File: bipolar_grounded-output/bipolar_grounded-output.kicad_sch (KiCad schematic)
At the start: 42 parts, among them J1 Conn_01x10_Pin, J10 Output, J11 Conn_Coaxial, J12 Conn_01x04_Pin, J2 Conn_01x10_Pin, J3 Conn_01x04_Pin, J4 Conn_01x05, J5 Conn_01x03, J6 Setpoint, J7 Monitor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

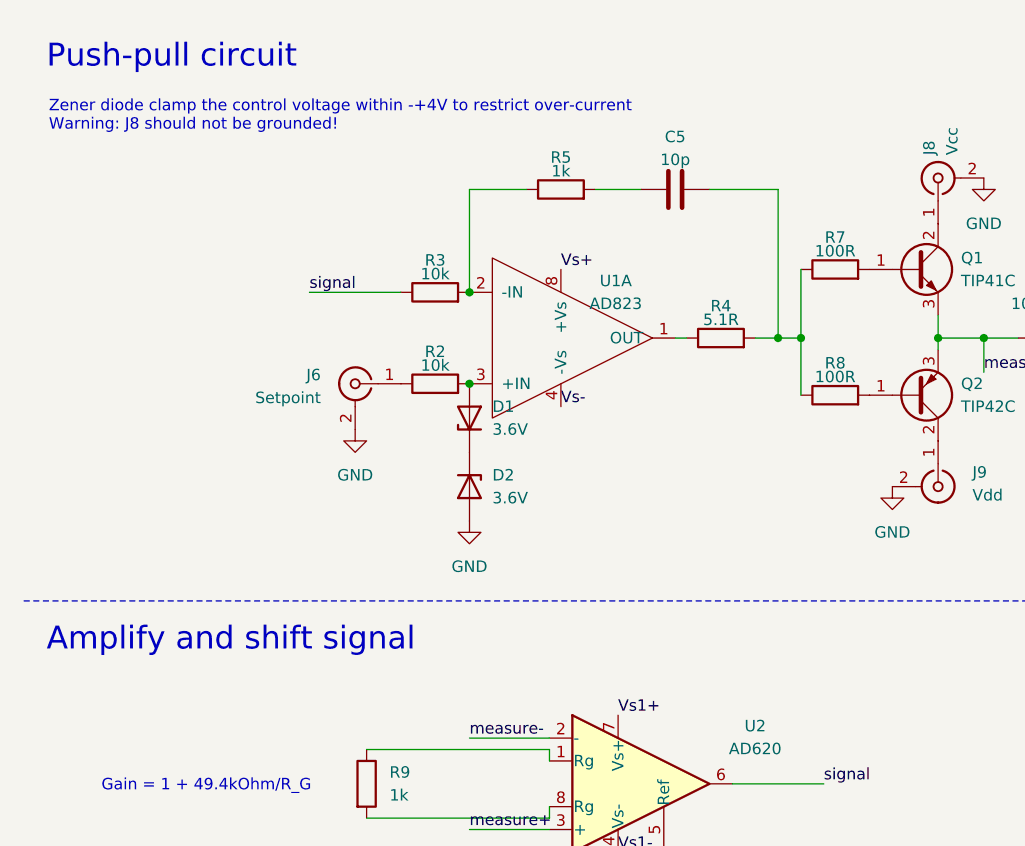
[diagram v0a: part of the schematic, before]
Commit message: add a grounded-output for bipolar current source
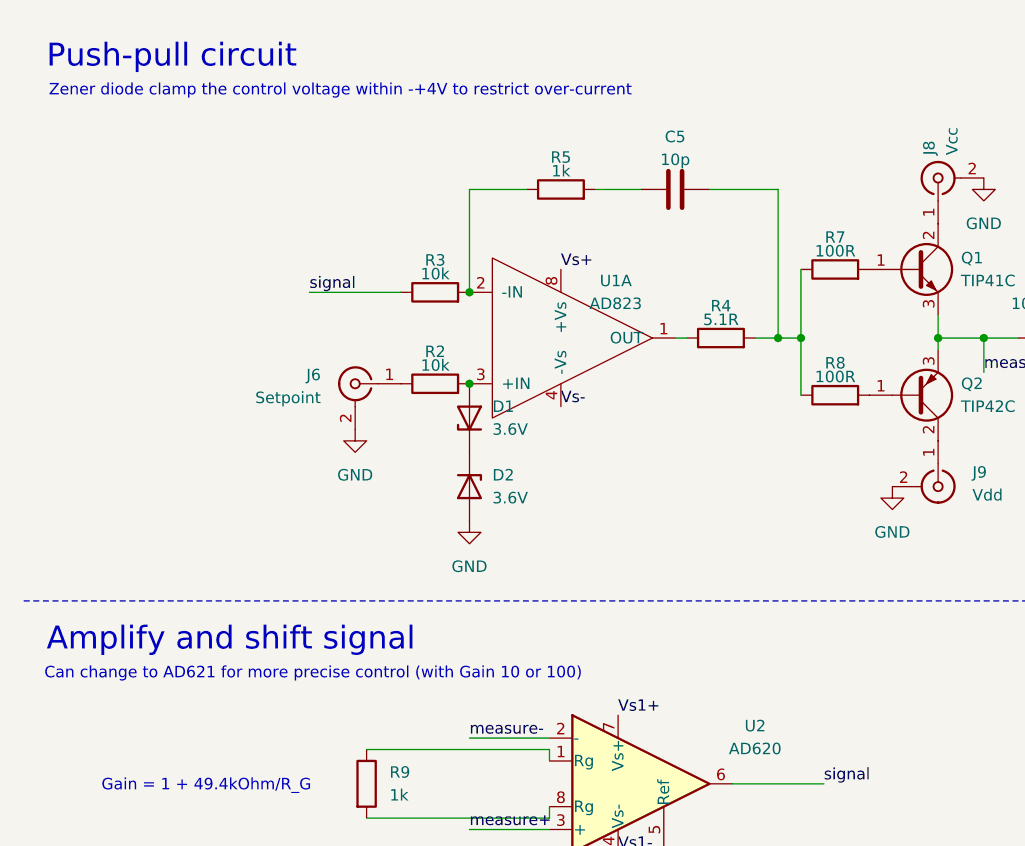
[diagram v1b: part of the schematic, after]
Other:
- note added: "Can change to AD621 for more precise control (with Gain 10 or 100)"
- note added: "Zener diode clamp the control voltage within -+4V to restrict over-current"
- note removed: "Zener diode clamp the control voltage within -+4V to restrict over-current Warning: J8 should not be grounded!"
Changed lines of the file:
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@@
 		)
 	)
-	(text "Zener diode clamp the control voltage within -+4V to restrict over-current\nWarning: J8 should not be grounded!"
+	(text "Zener diode clamp the control voltage within -+4V to restrict over-current"
 		(exclude_from_sim no)
-		(at 15.494 25.4 0)
+		(at 15.494 21.59 0)
 		(effects
 			(font
@@
 		(effects
 			(font
+				(size 1.27 1.27)
+			)
+			(justify left bottom)
+		)
+	)
+	(text "Can change to AD621 for more precise control (with Gain 10 or 100)"
+		(exclude_from_sim no)
+		(at 14.986 86.36 0)
+		(effects
+			(font

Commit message: layout PCB for grounded bipolar
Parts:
- removed J12, J3: Conn_01x04_Pin, Connector_JST:JST_PH_S4B-PH-K_1x04_P2.00mm_Horizontal, symbol Connector:Conn_01x04_Pin
- removed J5: Conn_01x03, Connector_Wire:SolderWire-0.75sqmm_1x03_P4.8mm_D1.25mm_OD2.3mm, symbol Connector_Generic:Conn_01x03
- added C10: 1n, Capacitor_THT:C_Disc_D5.0mm_W2.5mm_P5.00mm, symbol Device:C
- added J3: AD621 Gain or AD620 select Pin, Connector_PinHeader_2.54mm:PinHeader_1x03_P2.54mm_Vertical, symbol Connector:Conn_01x03_Pin
- added R10: 1k, Resistor_THT:R_Axial_DIN0207_L6.3mm_D2.5mm_P10.16mm_Horizontal, symbol Device:R
- D1, D2: value 3.6V -> 10V
- R1: footprint (none) -> Resistor_SMD:R_2512_6332Metric; LCSC (none) -> C500724
- R2: value 10k -> 1k; LCSC C57204 -> C57435
- R9: value 1k -> 510R; footprint (none) -> Resistor_THT:R_Axial_DIN0207_L6.3mm_D2.5mm_P10.16mm_Horizontal
- U2: footprint (none) -> Package_DIP:DIP-8_W7.62mm_Socket_LongPads
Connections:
- net GND: now also C10.1, R10.1
- net at R9.1: now also J3.1 (Pin_1); no longer U2.1 (Rg)
- net at R9.2, U2.8 (Rg): now also J3.3 (Pin_3)
- net at D1.2 (A), R2.2, U1.3 (+IN): now also C10.2
- net at J6.1 (In), R2.1: now also R10.2
- new net: J3.2 (Pin_2), U2.1 (Rg)
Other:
- note added: "AD620 Gain = 1 + 49.4kOhm/R_G, select 12 (for 510Ohm, Gain is around 100 -- 10V setpoint -> 1A current, can increase the resistor for larger current range); AD621 Gain = 10, do not connect; AD621 Gain = 100, select 23."
- note added: "Can change to AD621 for more precise control (with Gain 10 or 100). For AD621, use +-15V power supply instead of +-12V."
- note added: "Zener diode to clamp voltage can be choose based on needs. R2 and C10 forms a low pass filter around 100kHz"
- note removed: "Can change to AD621 for more precise control (with Gain 10 or 100)"
- note removed: "Gain = 1 + 49.4kOhm/R_G"
- note removed: "STEMMA QT I^{2}C connector"
- note removed: "Zener diode clamp the control voltage within -+4V to restrict over-current"
- moved on the sheet: C5, D1, D2, J10, J6, J8, J9, Q1, Q2, R1, R2, R3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

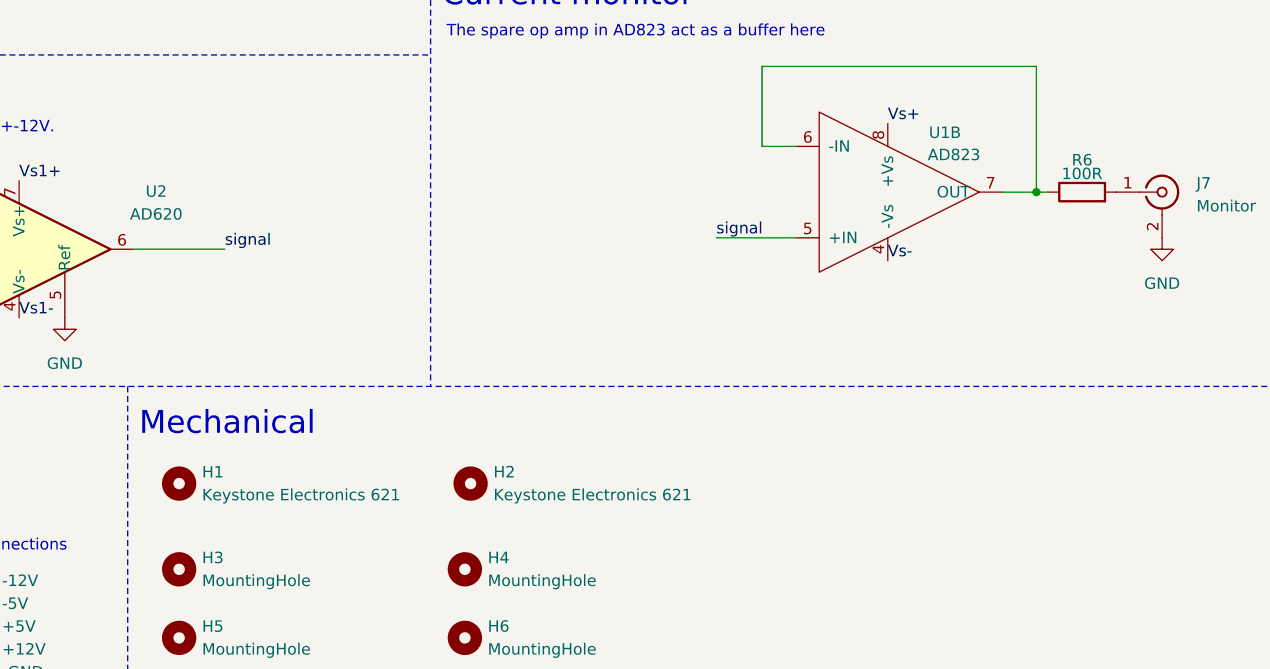
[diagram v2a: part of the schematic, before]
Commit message: update circuit with op amp power selection
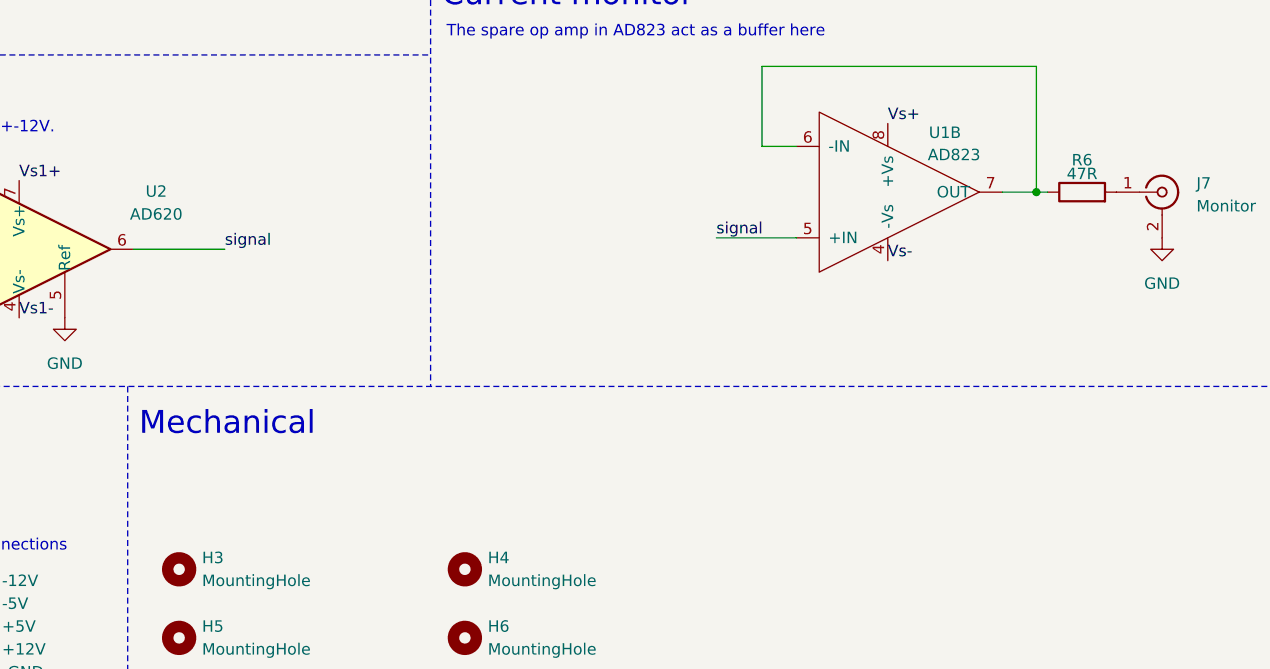
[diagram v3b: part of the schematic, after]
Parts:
- removed H1, H2: Keystone Electronics 621, matterwaves:Keystone 621, symbol Mechanical:MountingHole
- R6: value 100R -> 47R; LCSC C57438 -> C119296
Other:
- company: (none) -> Mueller Group, UC Berkeley
- title: ??? -> Bipolar current control (grounded output)
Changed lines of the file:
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@@
 	(paper "A4")
 	(title_block
-		(title "???")
-		(comment 1 "Designed by Jack Roth")
+		(title "Bipolar current control (grounded output)")
+		(company "Mueller Group, UC Berkeley")
 		(comment 2 "Compatible with Hammond Manufacturing series 1457")
 	)
@@
 	)
 	(symbol
-		(lib_id "Mechanical:MountingHole")
-		(at 169.545 125.095 0)
-		(unit 1)
-		(exclude_from_sim no)
-		(in_bom yes)
-		(on_board yes)
-		(dnp no)
-		(fields_autoplaced yes)
-		(property "Reference" "H2"
-			(at 172.085 123.825 0)
-			(effects
-				(font
-					(size 1.27 1.27)
-				)
-				(justify left)
-			)
-		)
-		(property "Value" "Keystone Electronics 621"
-			(at 172.085 126.365 0)
-			(effects
-				(font
-					(size 1.27 1.27)
-				)
-				(justify left)
-			)
-		)
-		(property "Footprint" "matterwaves:Keystone 621"
-			(at 169.545 125.095 0)
-			(effects
-				(font
-					(size 1.27 1.27)
-				)
-				(hide yes)
-			)
-		)
-		(property "Datasheet" "~"
-			(at 169.545 125.095 0)
-			(effects
-				(font
-					(size 1.27 1.27)
-				)
-				(hide yes)
-			)
-		)
-		(property "Description" "Mounting Hole without connection"
-			(at 169.545 125.095 0)
-			(effects
-				(font
-					(size 1.27 1.27)
-				)
-				(hide yes)
-			)
-		)
-		(property "Digikey PN" "36-621-ND"
-			(at 169.545 125.095 0)
-			(effects
-				(font
-					(size 1.27 1.27)
-				)
-				(hide yes)
-			)
-		)
-		(instances
-			(project "Hammond_1457_with_picoblade"
-				(path "/9c6abd11-1aac-4f08-8b79-cac116854bcb"
-					(reference "H2")
-					(unit 1)
-				)
-			)
-		)
-	)
-	(symbol
 		(lib_id "power:GND")
 		(at 62.23 60.96 0)
@@
 	)
 	(symbol
-		(lib_id "Mechanical:MountingHole")
-		(at 137.16 125.095 0)
-		(unit 1)
-		(exclude_from_sim no)
-		(in_bom yes)
-		(on_board yes)
-		(dnp no)
-		(fields_autoplaced yes)
-		(property "Reference" "H1"
-			(at 139.7 123.825 0)
-			(effects
-				(font
-					(size 1.27 1.27)
-				)
-				(justify left)
-			)
-		)
-		(property "Value" "Keystone Electronics 621"
-			(at 139.7 126.365 0)
-			(effects
-				(font
-					(size 1.27 1.27)
-				)
-				(justify left)
-			)
-		)
-		(property "Footprint" "matterwaves:Keystone 621"
-			(at 137.16 125.095 0)
-			(effects
-				(font
-					(size 1.27 1.27)
-				)
-				(hide yes)
-			)
-		)
-		(property "Datasheet" "~"
-			(at 137.16 125.095 0)
-			(effects
-				(font
-					(size 1.27 1.27)
-				)
-				(hide yes)
-			)
-		)
-		(property "Description" "Mounting Hole without connection"
-			(at 137.16 125.095 0)
-			(effects
-				(font
-					(size 1.27 1.27)
-				)
-				(hide yes)
-			)
-		)
-		(property "Digikey PN" "36-621-ND"
-			(at 137.16 125.095 0)
-			(effects
-				(font
-					(size 1.27 1.27)
-				)
-				(hide yes)
-			)
-		)
-		(instances
-			(project "Hammond_1457_with_picoblade"
-				(path "/9c6abd11-1aac-4f08-8b79-cac116854bcb"
-					(reference "H1")
-					(unit 1)
-				)
-			)
-		)
-	)
-	(symbol
 		(lib_id "power:GND")
 		(at 26.67 151.13 90)
@@
 			)
 		)
-		(property "Value" "100R"
+		(property "Value" "47R"
 			(at 237.49 90.678 90)
 			(effects
@@
 			)
 		)
-		(property "LCSC" "C57438"
+		(property "LCSC" "C119296"
 			(at 237.49 92.71 0)
 			(effects
